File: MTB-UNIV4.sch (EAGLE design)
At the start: 132 parts, among them IC1 MEGA128-A, IC2 SN75176BP, IC3 MC7805CDTG, IC4 ULN2803A, IC5 ULN2803A, Q1 14.7456 MHz, X1A ARK500/2, X1B ARK500/2, X2A ARK500/2, X2B ARK500/2, X3 1751316, X4 1751316, X5 1751316, X6 1751316

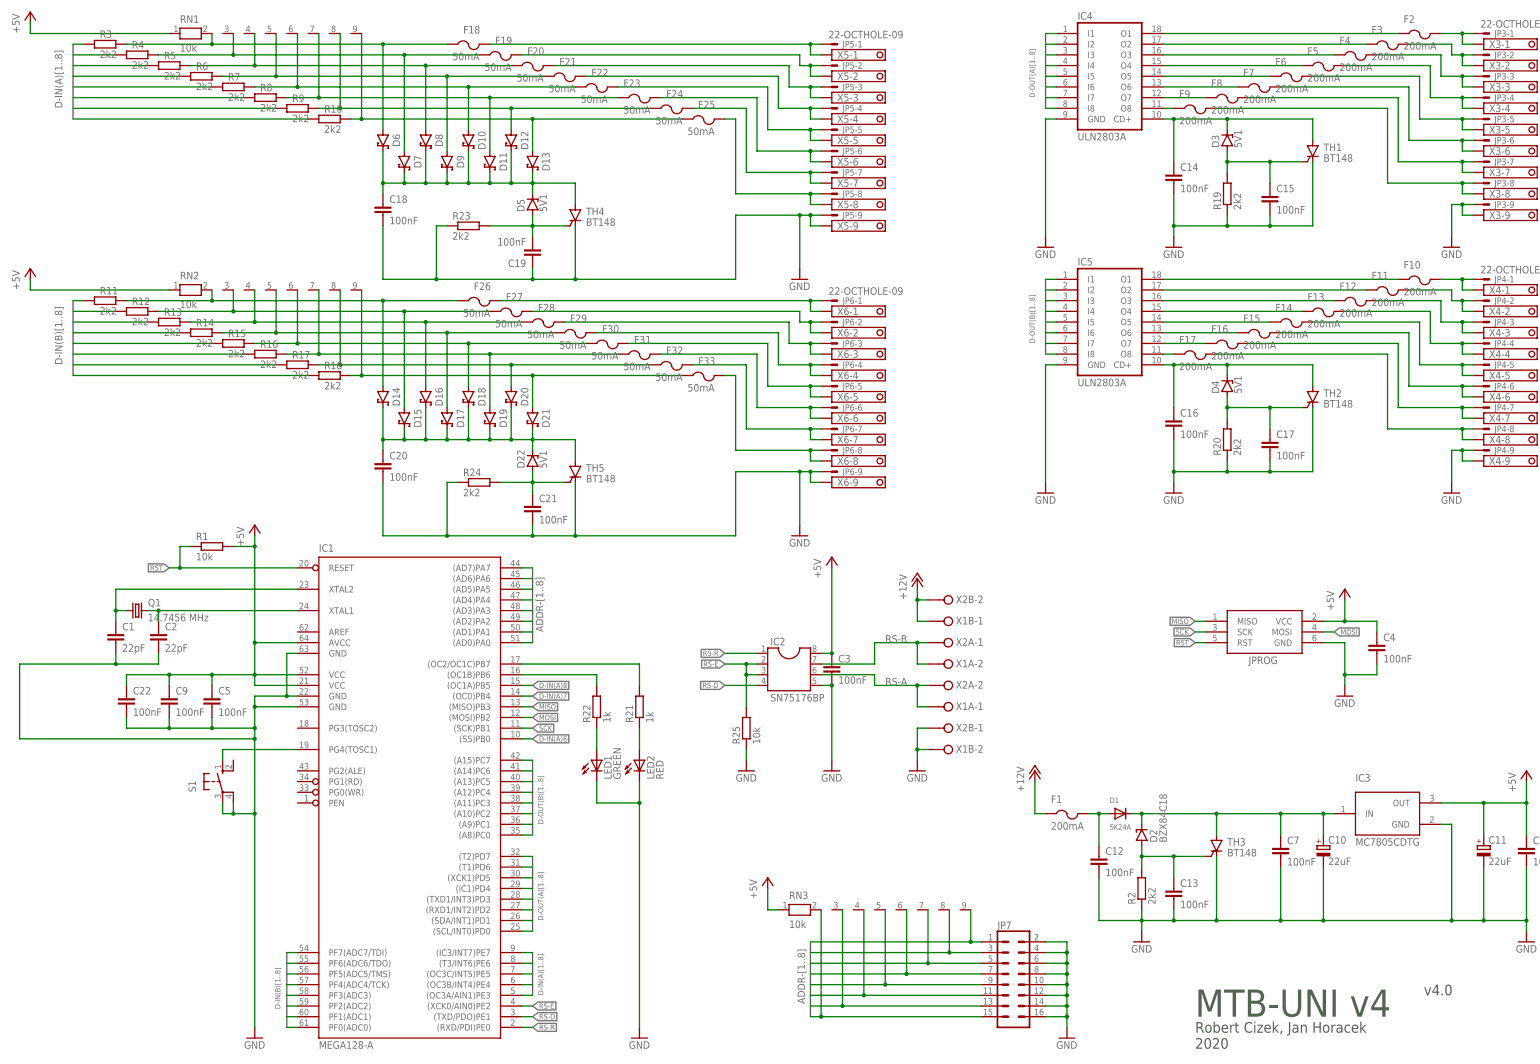
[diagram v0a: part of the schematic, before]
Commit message: Use BAT54C diodes.
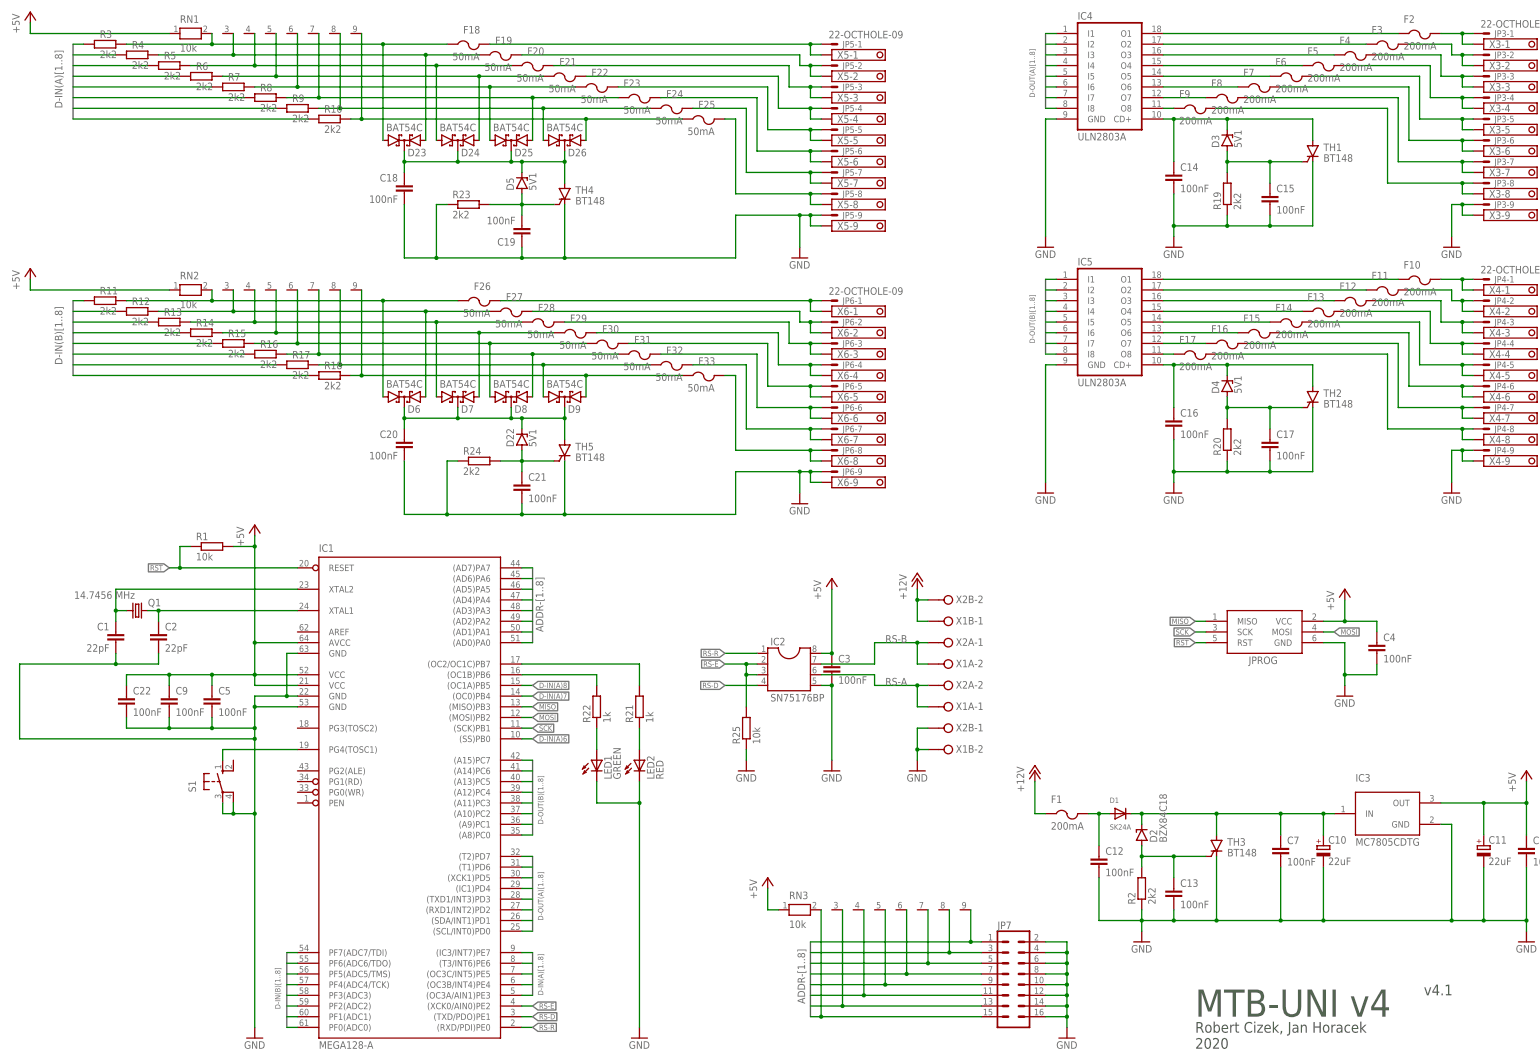
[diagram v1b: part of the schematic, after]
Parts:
- removed D10, D11, D12, D13, D14, D15, D16, D17, D18, D19, D20, D21: LM5819, ElectroKrt:SCHOTTKY_LM5819
- added D23, D24, D25, D26: BAT54C, diode:BAT54C
- D6, D7, D8, D9: value LM5819 -> BAT54C; device ElectroKrt:SCHOTTKY_LM5819 -> diode:BAT54C
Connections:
- net N$62: now also D23.A1; no longer D6.A
- net N$63: now also D23.A2; no longer D7.A
- net N$64: now also D24.A1; no longer D8.A
- net N$65: now also D24.A2; no longer D9.A
- net N$66: now also D25.A1; no longer D10.A
- net N$67: now also D25.A2; no longer D11.A
- net N$68: now also D26.A1; no longer D12.A
- net N$69: now also D26.A2; no longer D13.A
- net N$70: now also D23.CC, D24.CC, D25.CC, D26.CC; no longer D10.C, D11.C, D12.C, D13.C, D6.C, D7.C, D8.C, D9.C
- net N$72: now also D6.A1; no longer D14.A
- net N$73: now also D6.A2; no longer D15.A
- net N$74: now also D7.A1; no longer D16.A
- net N$75: now also D7.A2; no longer D17.A
- net N$76: now also D8.A1; no longer D18.A
- net N$77: now also D8.A2; no longer D19.A
- net N$78: now also D9.A1; no longer D20.A
- net N$79: now also D9.A2; no longer D21.A
- net N$80: now also D6.CC, D7.CC, D8.CC, D9.CC; no longer D14.C, D15.C, D16.C, D17.C, D18.C, D19.C, D20.C, D21.C
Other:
- note added: "v4.1"
- note removed: "v4.0"
- moved on the sheet: C18, C19, C20, C21, D22, D5, R23, R24, TH4, TH5

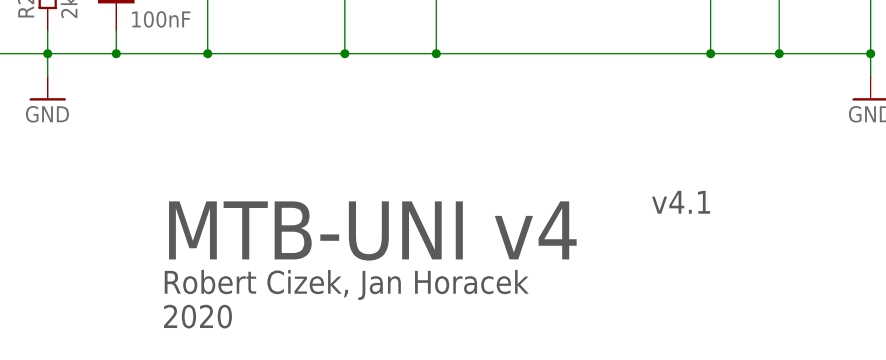
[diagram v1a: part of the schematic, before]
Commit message: Use vector font in schematics, use diacritics.
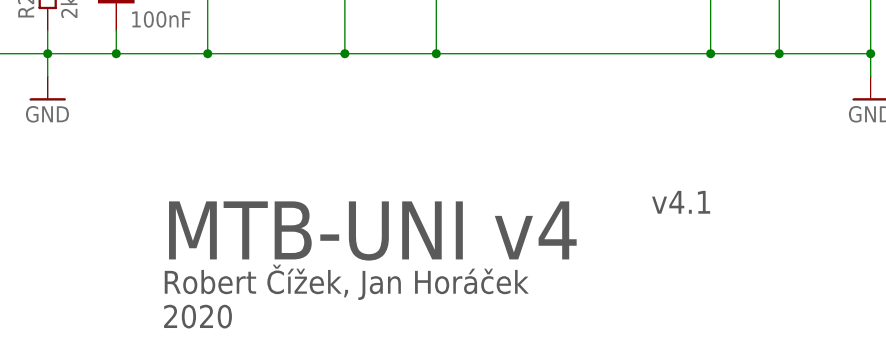
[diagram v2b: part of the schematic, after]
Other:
- note added: "Robert Čížek, Jan Horáček 2020"
- note removed: "Robert Cizek, Jan Horacek 2020"
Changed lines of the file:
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@@
 <drawing>
 <settings>
-<setting alwaysvectorfont="no"/>
+<setting alwaysvectorfont="yes"/>
 <setting verticaltext="up"/>
 </settings>
@@
 <plain>
 <text x="289.56" y="15.24" size="6.4516" layer="97">MTB-UNI v4</text>
-<text x="289.56" y="7.62" size="2.54" layer="97">Robert Cizek, Jan Horacek
+<text x="289.56" y="7.62" size="2.54" layer="97">Robert Čížek, Jan Horáček
 2020</text>
 <text x="343.916" y="20.32" size="2.54" layer="97">v4.1</text>

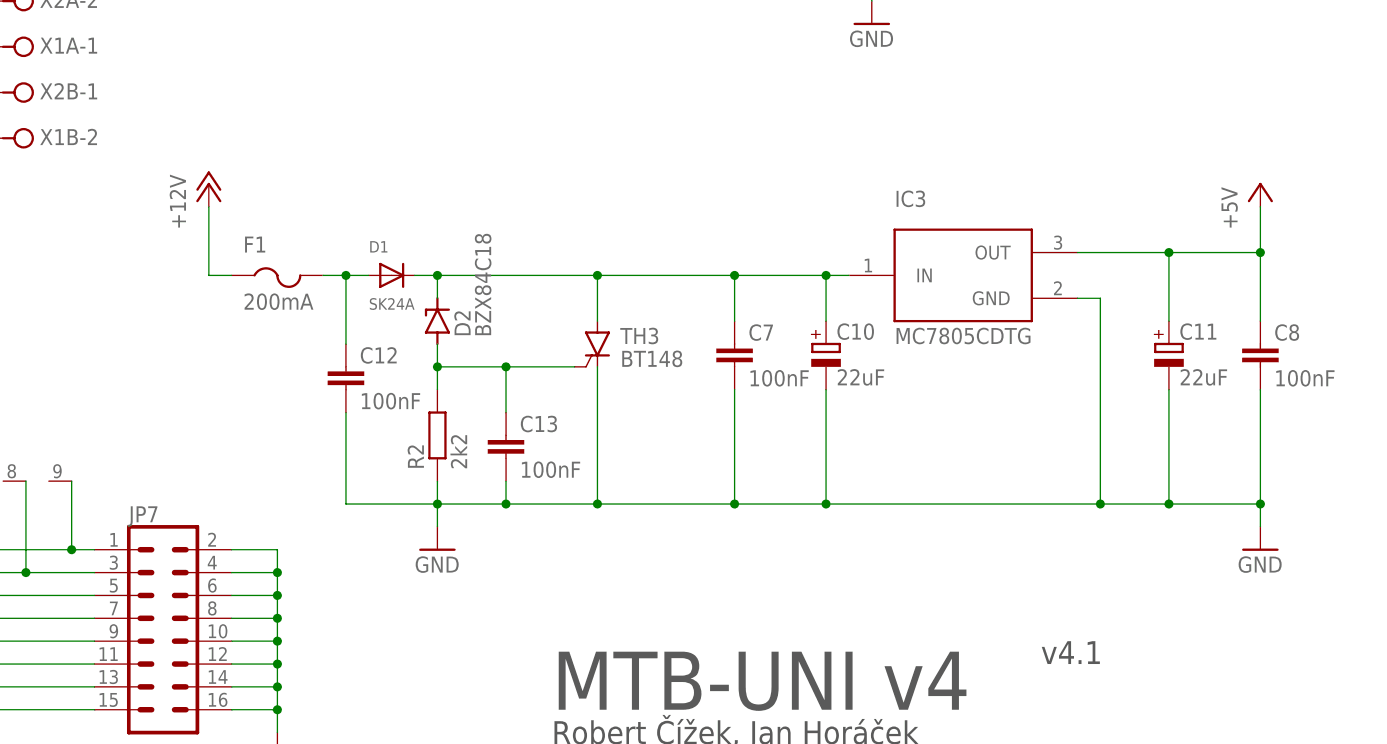
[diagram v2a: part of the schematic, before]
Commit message: Use ceramic capacitors only.
Reduce parts count.
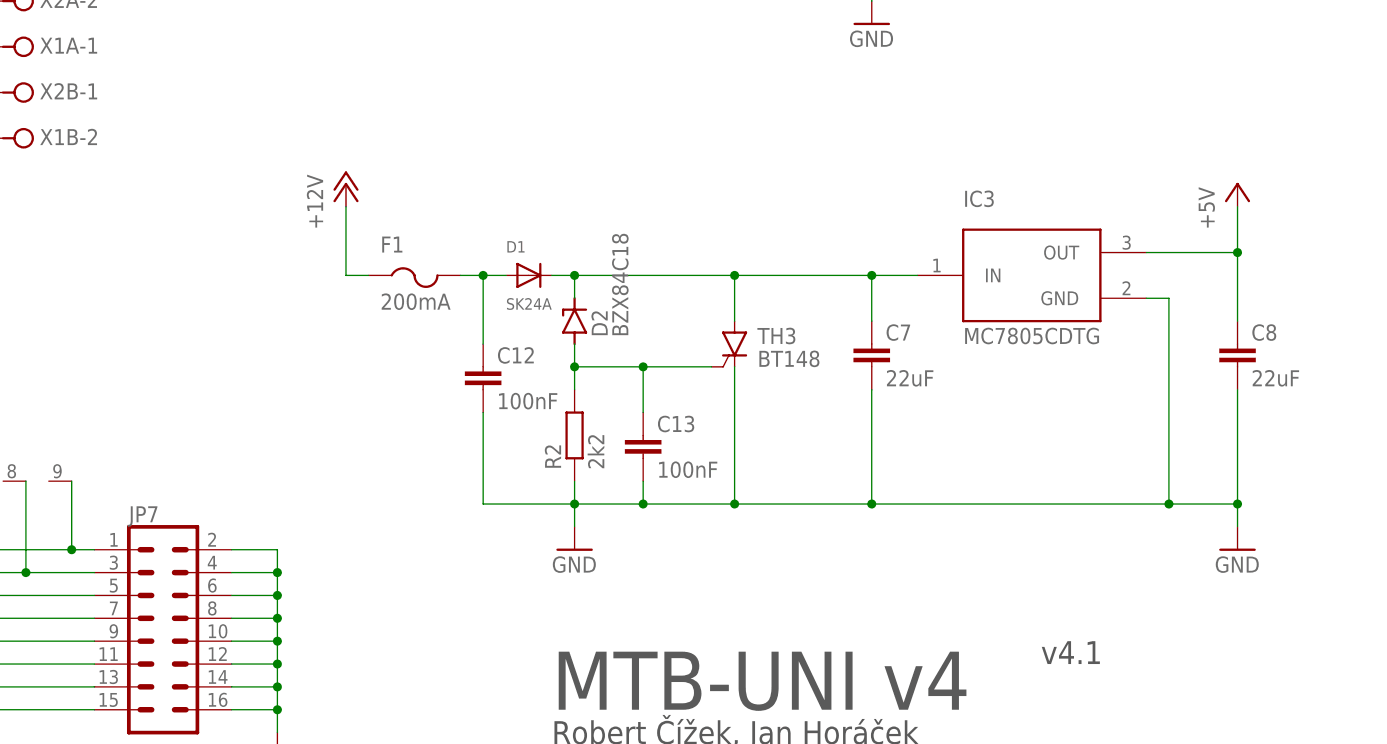
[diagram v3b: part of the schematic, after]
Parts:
- removed C10: 22uF, rcl:CPOL-EUSMCD
- removed C11: 22uF, rcl:CPOL-EUSMCB
- C7, C8: value 100nF -> 22uF
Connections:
- net +5V: no longer C11.+
- net GND: no longer C10.-, C11.-
- net N$13: no longer C10.+
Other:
- moved on the sheet: C12, C13, C7, C8, D1, D2, F1, IC3, R2, TH3

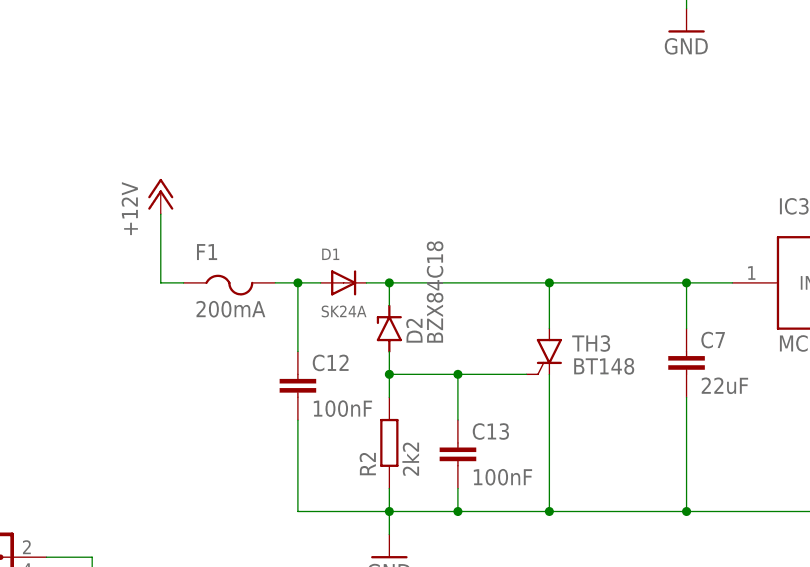
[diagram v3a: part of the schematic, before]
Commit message: Use diode available at JLCPCB as basic part.
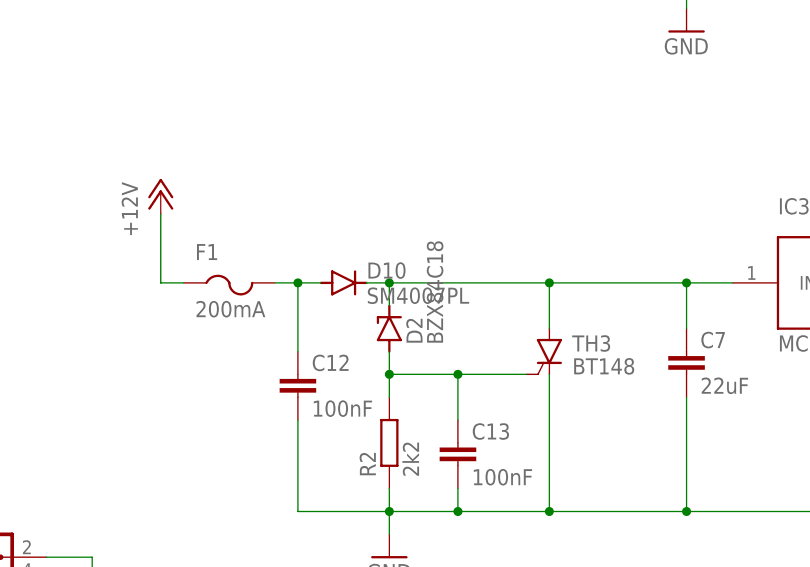
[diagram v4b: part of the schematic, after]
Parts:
- removed D1: SK24A, adafruit:DIODESMA
- added D10: SM4007PL, diode:CGRM4007-G
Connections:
- net N$13: now also D10.C; no longer D1.C
- net N$58: now also D10.A; no longer D1.A
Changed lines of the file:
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@@
 <part name="GND13" library="supply1" library_urn="urn:adsk.eagle:library:371" deviceset="GND" device=""/>
 <part name="GND14" library="supply1" library_urn="urn:adsk.eagle:library:371" deviceset="GND" device=""/>
-<part name="D1" library="adafruit" library_urn="urn:adsk.eagle:library:420" deviceset="DIODE" device="SMA" package3d_urn="urn:adsk.eagle:package:6240747/1" value="SK24A"/>
 <part name="F1" library="adafruit_edited" deviceset="PTCFUSE" device="-1206" value="200mA"/>
 <part name="FRAME1" library="frames" library_urn="urn:adsk.eagle:library:229" deviceset="A3L-LOC" device=""/>
@@
 <part name="D8" library="diode" library_urn="urn:adsk.eagle:library:210" deviceset="BAT54C" device="" package3d_urn="urn:adsk.eagle:package:43389/2"/>
 <part name="D9" library="diode" library_urn="urn:adsk.eagle:library:210" deviceset="BAT54C" device="" package3d_urn="urn:adsk.eagle:package:43389/2"/>
+<part name="D10" library="diode" library_urn="urn:adsk.eagle:library:210" deviceset="CGRM400*-G" device="" package3d_urn="urn:adsk.eagle:package:43457/2" technology="7" value="SM4007PL"/>
 </parts>
 <sheets>
@@
 <attribute name="VALUE" x="363.22" y="30.48" size="1.778" layer="96"/>
 </instance>
-<instance part="D1" gate="G$1" x="287.02" y="63.5" smashed="yes">
-<attribute name="NAME" x="284.48" y="66.04" size="1.27" layer="95"/>
-<attribute name="VALUE" x="284.48" y="59.69" size="1.27" layer="96"/>
-</instance>
 <instance part="F1" gate="G$1" x="274.32" y="60.96" smashed="yes">
 <attribute name="VALUE" x="270.51" y="59.69" size="1.778" layer="96"/>
@@
 <attribute name="NAME" x="140.462" y="160.5534" size="1.778" layer="95" rot="MR180"/>
 <attribute name="VALUE" x="135.382" y="166.5224" size="1.778" layer="96" rot="MR180"/>
+</instance>
+<instance part="D10" gate="G$1" x="287.02" y="63.5" smashed="yes">
+<attribute name="NAME" x="289.56" y="63.9826" size="1.778" layer="95"/>
+<attribute name="VALUE" x="289.56" y="61.1886" size="1.778" layer="96"/>
 </instance>
 </instances>
@@
 <junction x="325.12" y="63.5"/>
 <junction x="309.88" y="63.5"/>
-<pinref part="D1" gate="G$1" pin="C"/>
 <wire x1="289.56" y1="63.5" x2="292.1" y2="63.5" width="0.1524" layer="91"/>
 <junction x="292.1" y="63.5"/>
 <pinref part="D2" gate="G$1" pin="C"/>
 <pinref part="IC3" gate="G$1" pin="IN"/>
+<pinref part="D10" gate="G$1" pin="C"/>
 </segment>
 </net>
@@
 <pinref part="C12" gate="G$1" pin="1"/>
 <wire x1="281.94" y1="55.88" x2="281.94" y2="63.5" width="0.1524" layer="91"/>
-<pinref part="D1" gate="G$1" pin="A"/>
 <wire x1="284.48" y1="63.5" x2="281.94" y2="63.5" width="0.1524" layer="91"/>
 <junction x="281.94" y="63.5"/>
-</segment>
-</net>
+<pinref part="D10" gate="G$1" pin="A"/>
+</segment>
+</net>

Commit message: Use proper sockets (MVE252-5-V).
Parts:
- X1A, X1B, X2A, X2B: value ARK500/2 -> MVE252-5-V; device con-malina:ARK500/2 -> con-malina:MVE252-5-V
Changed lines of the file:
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@@
 <layer number="113" name="ReferenceLS" color="7" fill="1" visible="no" active="no"/>
 <layer number="118" name="Rect_Pads" color="7" fill="1" visible="no" active="no"/>
+<layer number="146" name="MillingKrab" color="11" fill="1" visible="yes" active="yes"/>
 <layer number="153" name="FabDoc1" color="6" fill="1" visible="no" active="no"/>
 <layer number="154" name="FabDoc2" color="2" fill="1" visible="no" active="no"/>
@@
 <part name="P+2" library="supply1" library_urn="urn:adsk.eagle:library:371" deviceset="+12V" device=""/>
 <part name="C22" library="rcl" deviceset="C-EU" device="C1206" value="100nF"/>
-<part name="X2B" library="con-malina" deviceset="ARK500/2" device=""/>
-<part name="X2A" library="con-malina" deviceset="ARK500/2" device=""/>
-<part name="X1A" library="con-malina" deviceset="ARK500/2" device=""/>
-<part name="X1B" library="con-malina" deviceset="ARK500/2" device=""/>
+<part name="X2B" library="con-malina" deviceset="MVE252-5-V" device=""/>
+<part name="X2A" library="con-malina" deviceset="MVE252-5-V" device=""/>
+<part name="X1A" library="con-malina" deviceset="MVE252-5-V" device=""/>
+<part name="X1B" library="con-malina" deviceset="MVE252-5-V" device=""/>
 <part name="R25" library="rcl" deviceset="R-EU_" device="R1206" value="10k"/>
 <part name="GND7" library="supply1" library_urn="urn:adsk.eagle:library:371" deviceset="GND" device=""/>
